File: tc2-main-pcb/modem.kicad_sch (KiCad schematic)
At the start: 34 parts, among them J111 Conn_01x08, J112 Screw_Terminal_01x01, U115 TPS6302x, U116 SIM7600G-H-M.2

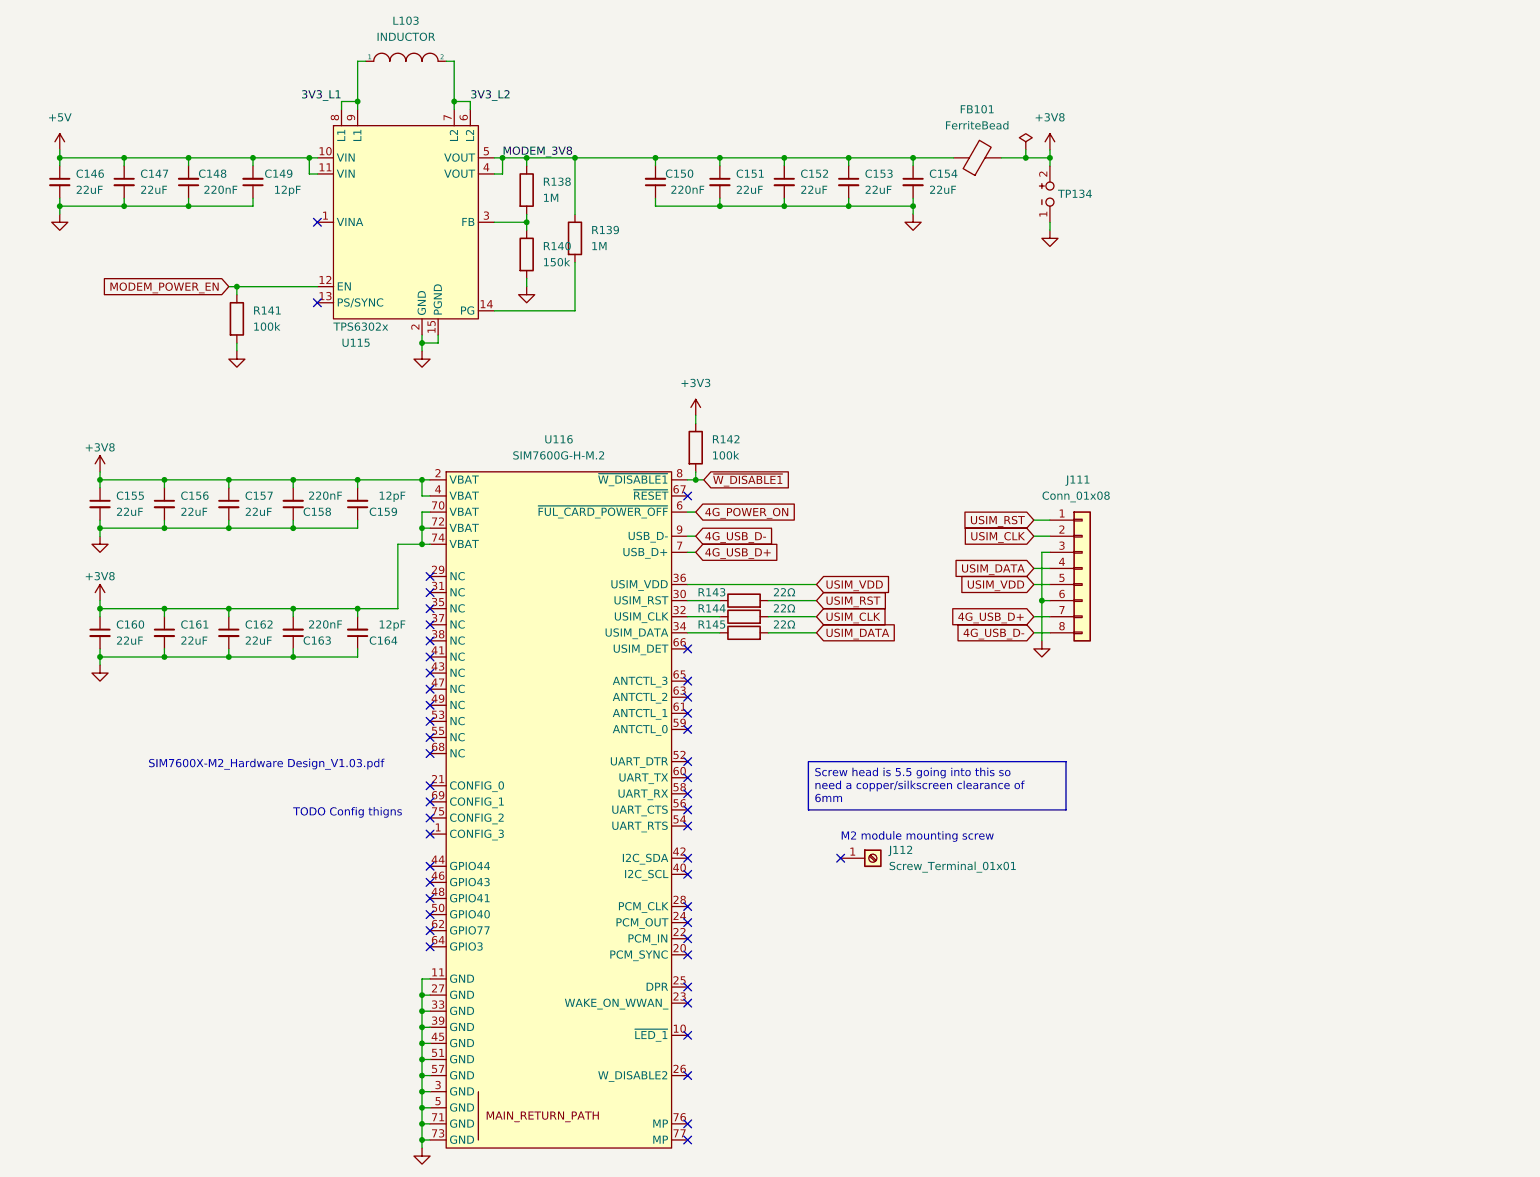
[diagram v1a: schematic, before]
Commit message: Update DC-DC converters
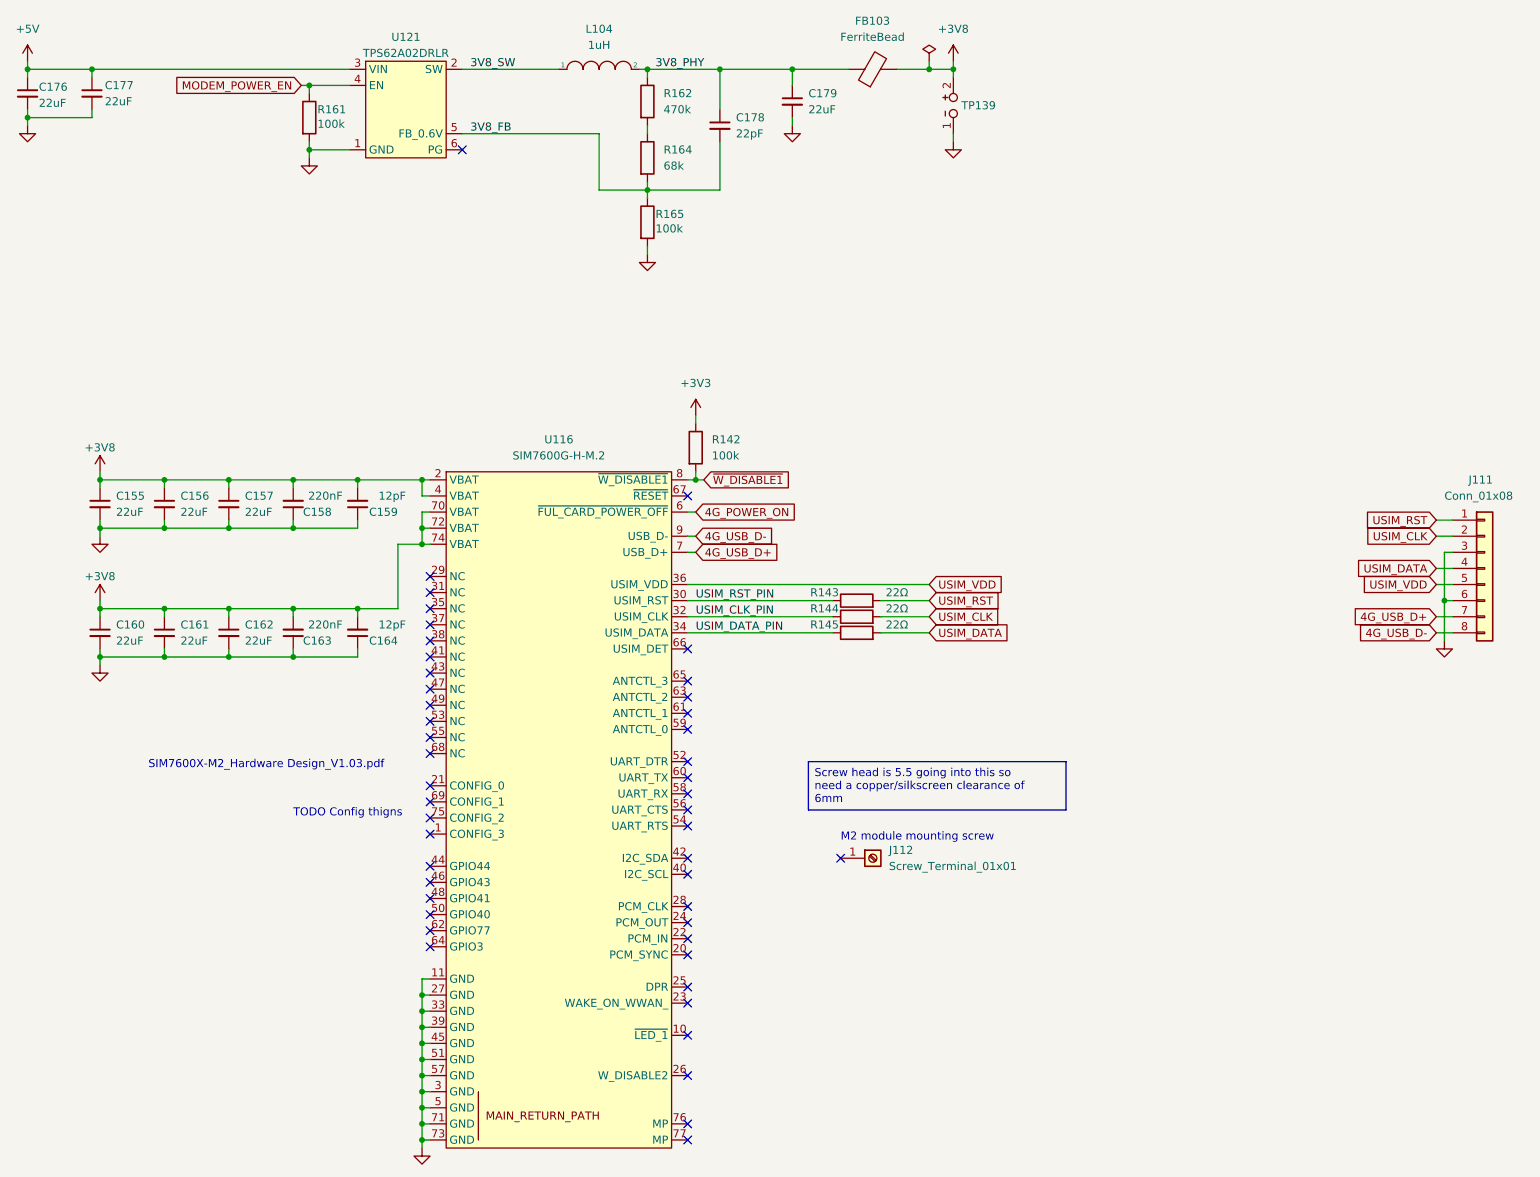
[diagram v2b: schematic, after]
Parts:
- removed C146, C147, C151, C152, C153, C154: 22uF, Capacitor_SMD:C_0603_1608Metric, symbol Device:C_Small
- removed C148, C150: 220nF, Capacitor_SMD:C_0402_1005Metric, symbol Device:C_Small
- removed C149: 12pF, Capacitor_SMD:C_0402_1005Metric, symbol Device:C_Small
- removed FB101: FerriteBead, Inductor_SMD:L_0805_2012Metric, symbol Device:FerriteBead
- removed L103: INDUCTOR, Inductor_SMD:L_1008_2520Metric, symbol cacophony-library:Power_Inductor
- removed R138, R139: 1M, Resistor_SMD:R_0402_1005Metric, symbol Device:R
- removed R140: 150k, Resistor_SMD:R_0402_1005Metric, symbol Device:R
- removed R141: 100k, Resistor_SMD:R_0402_1005Metric, symbol Device:R
- removed TP134: TP_2P, cacophony-library:test-point-2p, symbol cacophony-library:TestPoint_2Pole
- removed U115: TPS6302x, cacophony-library:VSON-14_L4.0-W3.0-P0.50-BL-EP_TI_DSJ, symbol cacophony-library:TPS6302x
- added C176, C177, C179: 22uF, Capacitor_SMD:C_0603_1608Metric, symbol Device:C_Small
- added C178: 22pF, Capacitor_SMD:C_0402_1005Metric, symbol Device:C_Small
- added FB103: FerriteBead, Inductor_SMD:L_0805_2012Metric, symbol Device:FerriteBead
- added L104: 1uH, Inductor_SMD:L_1008_2520Metric, symbol cacophony-library:Power_Inductor
- added R161, R165: 100k, Resistor_SMD:R_0402_1005Metric, symbol Device:R
- added R162: 470k, Resistor_SMD:R_0402_1005Metric, symbol Device:R
- added R164: 68k, Resistor_SMD:R_0402_1005Metric, symbol Device:R
- added TP139: TP_2P, cacophony-library:test-point-2p, symbol cacophony-library:TestPoint_2Pole
- added U121: TPS62A02DRLR, cacophony-library:SOT-563, symbol cacophony-library:TPS62A02DRLR
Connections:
- net +3V8: now also FB103.2, TP139.2
- net +5V: now also C176.1, C177.1, U121.3 (VIN)
- net GND: now also C176.2, C177.2, C179.2, R161.2, R165.2, TP139.1, U121.1 (GND)
- net MODEM_POWER_EN: now also R161.1, U121.4 (EN)
- net USIM_CLK_PIN: now reaches R144.1, U116.32 (USIM_CLK)
- net USIM_DATA_PIN: now reaches R145.1, U116.34 (USIM_DATA)
- net USIM_RST_PIN: now reaches R143.1, U116.30 (USIM_RST)
- new net: R162.2, R164.1
- new net 3V8_FB: C178.2, R164.2, R165.1, U121.5 (FB_0.6V)
- new net 3V8_PHY: C178.1, C179.1, FB103.1, L104.2, R162.1
- new net 3V8_SW: L104.1, U121.2 (SW)
- no-connect marks 48 -> 47
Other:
- moved on the sheet: J111, R143, R144, R145

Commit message: Update schematic
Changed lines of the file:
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@@
 			)
 		)
-		(property "Description" ""
+		(property "Description" "Unpolarized capacitor, small symbol"
 			(at 60.96 92.71 0)
 			(hide yes)
@@
 			)
 		)
-		(property "Description" ""
+		(property "Description" "Unpolarized capacitor, small symbol"
 			(at 40.64 113.03 0)
 			(hide yes)
